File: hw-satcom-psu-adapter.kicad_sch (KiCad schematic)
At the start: 25 parts

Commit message: pmbus and normal
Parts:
- C1: value (none) -> 400uF/100V; footprint (none) -> Capacitor_THT:C_Disc_D5.0mm_W2.5mm_P5.00mm
- C2: value (none) -> 470uF/50V
- C3: value (none) -> 470uF/50V; footprint (none) -> Capacitor_THT:C_Disc_D5.0mm_W2.5mm_P5.00mm
- C4: value (none) -> 1uF/50V; footprint (none) -> Capacitor_SMD:C_0805_2012Metric
- D1: value (none) -> Yellow; footprint (none) -> LED_SMD:LED_0603_1608Metric
- D2, D3: footprint (none) -> LED_SMD:LED_0603_1608Metric
- F1: value (none) -> 10A; footprint (none) -> Fuse:Fuse_1206_3216Metric
- H1: value (none) -> MountingHole; footprint (none) -> MountingHole:MountingHole_2.5mm
- J1: value (none) -> Conn_01x04; footprint (none) -> Connector_PinSocket_2.54mm:PinSocket_1x04_P2.54mm_Vertical
- J2, J3: value (none) -> XT30; footprint (none) -> Connector_AMASS:AMASS_XT30PW-M_1x02_P2.50mm_Horizontal
- J4: value (none) -> Conn_01x06_MountingPin; footprint (none) -> Connector_Molex:Molex_CLIK-Mate_502382-0670_1x06-1MP_P1.25mm_Vertical
- J5: value (none) -> s; footprint (none) -> Connector_Molex:Molex_CLIK-Mate_502382-0370_1x03-1MP_P1.25mm_Vertical
- R1: value (none) -> 4.7k; footprint (none) -> Resistor_SMD:R_0603_1608Metric
- R10, R7, R8, R9: value (none) -> NC; footprint (none) -> Resistor_SMD:R_0603_1608Metric
- R2, R3: footprint (none) -> Resistor_SMD:R_0603_1608Metric
- R4: value (none) -> 3.9k; footprint (none) -> Resistor_SMD:R_0603_1608Metric
- R5: value (none) -> 100k; footprint (none) -> Resistor_SMD:R_0603_1608Metric
- R6: value (none) -> 47k; footprint (none) -> Resistor_SMD:R_0603_1608Metric
- U1: value (none) -> Brick-DCDC; footprint (none) -> alex's:Quarter-Brick-PMBus

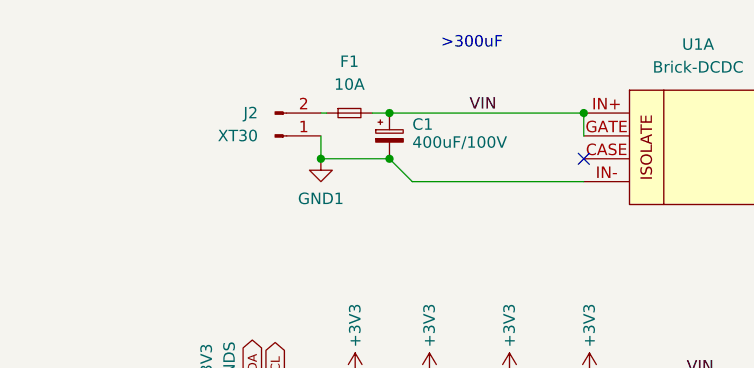
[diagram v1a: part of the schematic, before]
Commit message: change fuse footprint
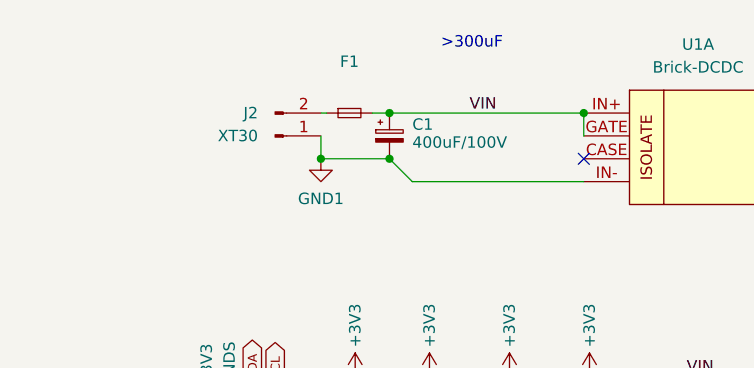
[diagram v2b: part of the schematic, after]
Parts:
- F1: value 10A -> (none); footprint Fuse:Fuse_1206_3216Metric -> (none)
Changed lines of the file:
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@@
     (in_bom yes) (on_board yes) (fields_autoplaced)
     (property "Reference" "F1" (id 0) (at 92.71 96.52 0))
-    (property "Value" "10A" (id 1) (at 92.71 99.06 0))
-    (property "Footprint" "Fuse:Fuse_1206_3216Metric" (id 2) (at 92.71 102.235 0)
+    (property "Value" "" (id 1) (at 92.71 99.06 0))
+    (property "Footprint" "" (id 2) (at 92.71 102.235 0)
       (effects (font (size 1.27 1.27)) hide)
     )
@@
     )
     (path "/3d21ad1e-adf2-4a6f-b9bb-fd727992bece"
-      (reference "F1") (unit 1) (value "10A") (footprint "Fuse:Fuse_1206_3216Metric")
+      (reference "F1") (unit 1) (value "10A") (footprint "Fuse:Fuse_2512_6332Metric")
     )
     (path "/d06f684c-b86b-49a5-ad3a-2b8c544739e6"

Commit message: Temp
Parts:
- removed D3: Yellow, LED_SMD:LED_0603_1608Metric, symbol Device:LED
- removed J2, J3: XT30, Connector_AMASS:AMASS_XT30PW-M_1x02_P2.50mm_Horizontal, symbol Connector:Conn_01x02_Male
- removed J4: Conn_01x06_MountingPin, Connector_Molex:Molex_CLIK-Mate_502382-0670_1x06-1MP_P1.25mm_Vertical, symbol Connector_Generic_MountingPin:Conn_01x06_MountingPin
- removed R5: 100k, Resistor_SMD:R_0603_1608Metric, symbol Device:R
- removed R6: 47k, Resistor_SMD:R_0603_1608Metric, symbol Device:R
- added C5: 47nF, lc:0402_C, symbol Device:C_Small
- added C6: 10nF, lc:0402_C, symbol Device:C_Small
- added D3: 1N4148WS, lc:SOD-323, symbol Diode:1N4148WS
- added D4, D5: Yellow, lc:0805_LED_S1_NUM, symbol Device:LED
- added D6, D7: 1N5819WS, lc:SOD-323, symbol Diode:1N4148WS
- added J2, J3, J4, J6, J8: Conn_01x04_Female, symbol Connector:Conn_01x04_Female
- added J7, J9: Conn_01x08_Female, symbol Connector:Conn_01x08_Female
- added Q1, Q2, Q3: NCE0140K2, Package_TO_SOT_SMD:TO-252-2, symbol Device:Q_NMOS_GDS
- added Q4, Q5: 2N7002, Package_TO_SOT_SMD:SOT-23, symbol Transistor_FET:2N7002
- added R11, R22: 8.2k, lc:0603_R, symbol Device:R_Small
- added R12, R17: 220k, lc:0603_R, symbol Device:R_Small
- added R13, R16, R18: 51k, lc:0603_R, symbol Device:R_Small
- added R14: 120k, lc:0603_R, symbol Device:R_Small
- added R15: 3m/1W, lc:2512_R, symbol Device:R_Small
- added R19, R23: 22k, lc:0603_R, symbol Device:R_Small
- added R20, R21: 5.1k, lc:0603_R, symbol Device:R_Small
- added R24: 10k, lc:0603_R, symbol Device:R_Small
- added R25: 390, lc:0603_R, symbol Device:R_Small
- added R26, R27: 100, lc:0603_R, symbol Device:R_Small
- added R5: 390k, lc:0603_R, symbol Device:R_Small
- added R6: 5.6k, lc:0603_R, symbol Device:R_Small
- added U10, U8, U9: ZXDN10, t123yh:ZXDN10, symbol t123yh:ZXDN10
- added U2: TPS2350, Package_SO:TSSOP-14_4.4x5mm_P0.65mm, symbol t123yh:TPS2350
- added U3, U4, U6: EL3H7(B)(TA)-G, Package_SO:SOP-4_4.4x2.6mm_P1.27mm, symbol Isolator:PC817
- added U5: AV10-48S05, t123yh:AV10-48Sxx, symbol t123yh:AV10-48S05
- added U7: TPS3510, Package_SO:SOIC-8_3.9x4.9mm_P1.27mm, symbol t123yh:TPS3510
- D2: value Yellow -> Red; footprint LED_SMD:LED_0603_1608Metric -> lc:0805_LED_S1_NUM
- F1: value (none) -> 10A; footprint (none) -> Fuse:Fuse_2512_6332Metric
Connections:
- net GND2: now also D5.1 (K), J8.1 (Pin_1), J8.2 (Pin_2), J8.3 (Pin_3), J8.4 (Pin_4), J9.1 (Pin_1), J9.2 (Pin_2), J9.3 (Pin_3), J9.4 (Pin_4), J9.5 (Pin_5), J9.6 (Pin_6), J9.7 (Pin_7), J9.8 (Pin_8), Q4.2 (S), Q5.2 (S), R19.2, R25.1, R26.1, R27.1, U10.3 (GND), U10.4 (GND), U4.2, U5.3 (-Vo), U7.2 (GND), U8.3 (GND), U8.4 (GND), U9.3 (GND), U9.4 (GND)
- net at J5.1 (Pin_1): no longer U1.6 (ISHARE)
- net at D2.1 (K): now also U2.2 (FLT)
- net GND1: no longer names the net of C1.2, U1.IN-
- net GND1: now also Q2.2 (D), R17.1, U5.1 (-Vin)
- removed net VIN: C1.1, D2.2 (A), F1.2, U1.GATE, U1.IN+
- net VOUT renamed +12V
- net +12V: now also D6.2 (A), J7.1 (Pin_1), J7.2 (Pin_2), J7.3 (Pin_3), J7.4 (Pin_4), J7.5 (Pin_5), J7.6 (Pin_6), J7.7 (Pin_7), J7.8 (Pin_8), R24.2, U10.2 (VIN), U8.2 (VIN), U9.2 (VIN)
- new net: D2.2 (A), R12.1
- new net: R18.1, U6.1
- new net: R27.2, U10.6 (ADJ)
- new net: Q5.3 (D), R24.1, U10.1 (EN), U8.1 (EN), U9.1 (EN)
- new net: R25.2, U8.6 (ADJ)
- new net: Q1.1 (G), U2.8 (GATEB)
- new net: C5.1, C6.1, D4.1 (K), Q1.2 (D), Q3.2 (D), R11.2, R15.2, U2.7 (SOURCE)
- new net: R11.1, R6.2, U2.4 (OV)
- new net: D3.1 (K), U2.1 (RTN)
- new net: R26.2, U9.6 (ADJ)
- new net: R17.2, U1.GATE, U3.3, U4.3
- new net: D6.1 (K), D7.1 (K), U7.7 (V_{DD})
- new net: D4.2 (A), R14.1
- new net: R16.2, U3.4, U4.4
- new net: Q2.3 (S), R15.1, U2.10 (SENSE)
- new net: D5.2 (A), R22.1
- new net: Q4.3 (D), R21.2, U7.1 (PGI)
- new net: Q2.1 (G), U2.11 (GAT)
- new net: R5.2, R6.1, U2.3 (UV)
- new net: C5.2, U2.5 (FLTTIM)
- new net: C6.2, U2.6 (RAMP)
- new net: Q3.1 (G), U2.9 (GATEA)
- new net: Q4.1 (G), R19.1, U6.3
- new net: R13.2, U3.1
- new net +3.3V: J6.1 (Pin_1), J6.2 (Pin_2), J6.3 (Pin_3), J6.4 (Pin_4), U7.5 (VS33), U8.5 (VOUT)
- new net +5VA: J3.1 (Pin_1), J3.2 (Pin_2), J3.3 (Pin_3), J3.4 (Pin_4), U7.6 (VS5), U9.5 (VOUT)
- new net +5VD: J4.1 (Pin_1), J4.2 (Pin_2), J4.3 (Pin_3), J4.4 (Pin_4), R23.1, U10.5 (VOUT)
- new net +5VSB: D7.2 (A), J2.1 (Pin_1), R20.1, R21.1, R22.2, U5.4 (+Vo), U6.4
- new net FPO: Q5.1 (G), R20.2, U4.1, U7.3 (~{FPO})
- new net NEGA: Q3.3 (S), U2.14 (-VINA)
- new net NEGB: Q1.3 (S), U2.13 (-VINB)
- new net PGOOD: J2.3 (Pin_3), R23.2, U7.8 (PGO)
- new net PG_HV: U2.12 (PG), U3.2, U6.2
- new net PSON: J2.2 (Pin_2), U7.4 (~{PSON})
- new net RET: C1.1, D3.2 (A), R12.2, R13.1, R14.2, R16.1, R18.2, R5.1, U1.IN+, U5.2 (+Vin)
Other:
- note added: "1W"
- note added: "Over voltage: 65V Under voltage: 41V"
- note added: "Pull up to always-on power"
- note added: "This octocoupler turns on when fault condition occurred downstream"
- note added: "This octocoupler turns on when power is not good"
- note added: "This octocoupler turns on when power is not good. When this happens, downstream PGOOD will be pulled low."
- note removed: ">1000uF"
- note removed: ">300uF"
- moved on the sheet: C1, C2, C3, C4, D1, H1, J1, J5, R1, R10, R2, R3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

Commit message: ATX
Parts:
- removed C2, C3: 470uF/50V, Capacitor_THT:C_Disc_D5.0mm_W2.5mm_P5.00mm, symbol Device:C_Polarized_Small
- removed C4: 1uF/50V, Capacitor_SMD:C_0805_2012Metric, symbol Device:C_Small
- removed F1: 10A, Fuse:Fuse_2512_6332Metric, symbol Device:Fuse_Small
- removed H1: MountingHole, MountingHole:MountingHole_2.5mm, symbol Mechanical:MountingHole
- removed J1: Conn_01x04, Connector_PinSocket_2.54mm:PinSocket_1x04_P2.54mm_Vertical, symbol Connector_Generic:Conn_01x04
- removed J2, J3, J4, J6, J8: Conn_01x04_Female, symbol Connector:Conn_01x04_Female
- removed J5: s, Connector_Molex:Molex_CLIK-Mate_502382-0370_1x03-1MP_P1.25mm_Vertical, symbol Connector_Generic_MountingPin:Conn_01x03_MountingPin
- removed J7, J9: Conn_01x08_Female, symbol Connector:Conn_01x08_Female
- removed R1, R2, R3: 4.7k, Resistor_SMD:R_0603_1608Metric, symbol Device:R
- removed R10, R9: NC, Resistor_SMD:R_0603_1608Metric, symbol Device:R_Small
- removed R4: 3.9k, Resistor_SMD:R_0603_1608Metric, symbol Device:R
- removed R7, R8: NC, Resistor_SMD:R_0603_1608Metric, symbol Device:R
- added C10, C12, C13, C15, C16, C17, C7, C8, C9: 470uF/25V, Capacitor_THT:CP_Radial_D6.3mm_P2.50mm, symbol Device:CP
- added C14: 100nF/100V, lc:0805_C, symbol Device:C_Small
- added D10, D8, D9: Green, lc:0805_LED_S1_NUM, symbol Device:LED
- added D11, D12: Blue, lc:0805_LED_S1_NUM, symbol Device:LED
- added FL1: ACM1513F-551T100, t123yh:ACM1513, symbol Device:Filter_EMI_LL_1423
- added H2, H3, H8, H9: SMTSO-M3, MountingHole:MountingHole_4.3mm_M4_Pad, symbol Mechanical:MountingHole
- added H4, H5, H6, H7: SMTSO-632, MountingHole:MountingHole_5.5mm_Pad, symbol Mechanical:MountingHole
- added J1, J5: Conn_01x02_Male, Connector_AMASS:AMASS_XT60-M_1x02_P7.20mm_Vertical, symbol Connector:Conn_01x02_Male
- added J2: ATX-24, t123yh:ATX-24P, symbol Connector:ATX-24
- added J3, J4: Conn_02x02_Top_Bottom, t123yh:ATX-4P, symbol Connector_Generic:Conn_02x02_Top_Bottom
- added J_CPU1, J_CPU2: Conn_02x04_Top_Bottom, t123yh:ATX-8P, symbol Connector_Generic:Conn_02x04_Top_Bottom
- added Q6: 2N7002, Package_TO_SOT_SMD:SOT-23, symbol Transistor_FET:2N7002
- added R1: 200k, lc:0402_R, symbol Device:R_Small
- added R2: 22k, lc:0402_R, symbol Device:R_Small
- added R3, R4: 56k, lc:0402_R, symbol Device:R_Small
- added R7, R8: 3.3k, lc:0402_R, symbol Device:R_Small
- D1: value Yellow -> Green; footprint LED_SMD:LED_0603_1608Metric -> lc:0805_LED_S1_NUM
- R11, R13, R19, R20, R21, R22, R23, R26, R27, R6: footprint lc:0603_R -> lc:0402_R
- R15: value 3m/1W -> 3m
- R16: value 51k -> 10k; footprint lc:0603_R -> lc:0402_R
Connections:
- net +12V: now also C10.1, C12.1, C13.1, C7.1, C8.1, J2.10 (+12V), J2.11 (+12V), J3.2 (Pin_2), J4.2 (Pin_2), J_CPU1.5 (Pin_5), J_CPU1.6 (Pin_6), J_CPU1.7 (Pin_7), J_CPU1.8 (Pin_8), J_CPU2.5 (Pin_5), J_CPU2.6 (Pin_6), J_CPU2.7 (Pin_7), J_CPU2.8 (Pin_8), R1.2
- net +3.3V: now also C15.1, J2.1 (+3.3V), J2.12 (+3.3V), J2.13 (+3.3V), J2.2 (+3.3V), R2.2
- net +5VA: now also R23.1, C16.1, J2.21 (+5V), J2.22 (+5V), J2.23 (+5V), J2.4 (+5V), J2.6 (+5V), R3.2, R7.2, R8.2
- net +5VD: now also C17.1, J3.3 (Pin_3), J4.3 (Pin_3), R4.2; no longer R23.1
- net +5VSB: now also C9.1, J2.9 (+5VSB)
- net GND2: now also D1.1 (K), C10.2, C12.2, C13.2, C15.2, C16.2, C17.2, C7.2, C8.2, C9.2, D10.1 (K), D8.1 (K), D9.1 (K), J2.15 (GND), J2.17 (GND), J2.18 (GND), J2.19 (GND), J2.24 (GND), J2.3 (GND), J2.5 (GND), J2.7 (GND), J3.1 (Pin_1), J3.4 (Pin_4), J4.1 (Pin_1), J4.4 (Pin_4), J_CPU1.1 (Pin_1), J_CPU1.2 (Pin_2), J_CPU1.3 (Pin_3), J_CPU1.4 (Pin_4), J_CPU2.1 (Pin_1), J_CPU2.2 (Pin_2), J_CPU2.3 (Pin_3), J_CPU2.4 (Pin_4), Q6.2 (S)
- net NEGA: now also J1.1 (Pin_1)
- net NEGB: now also J5.1 (Pin_1)
- net PGOOD: now also J2.8 (PWR_OK), Q6.1 (G)
- net PSON: now also D12.1 (K), J2.16 (PS_ON#)
- net NEG_FIL: now reaches C1.2, R17.1, U1.IN-, U5.1 (-Vin)
- net NEG_FIL: now also FL1.4; no longer Q2.2 (D)
- net DCDC_EN: now reaches Q5.3 (D), R24.1, U10.1 (EN), U8.1 (EN), U9.1 (EN)
- net NEG: now reaches C5.1, C6.1, D4.1 (K), Q1.2 (D), Q3.2 (D), R11.2, R15.2, U2.7 (SOURCE)
- net +3V3: no longer names the net of D1.2 (A)
- net +3V3: now also R1.1
- net RET renamed RTN
- net RTN: now also C14.1, FL1.2, J1.2 (Pin_2), J5.2 (Pin_2); no longer C1.1, R18.2, U1.IN+, U5.2 (+Vin)
- new net: D12.2 (A), R8.1
- new net: D8.2 (A), R2.1
- new net: D11.1 (K), Q6.3 (D)
- new net: D11.2 (A), R7.1
- new net: D10.2 (A), R4.1
- new net: D9.2 (A), R3.1
- new net NEG_SS: C14.2, FL1.1, Q2.2 (D)
- new net RTN_FIL: C1.1, FL1.3, R18.2, U1.IN+, U5.2 (+Vin)
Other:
- note added: "(back)"
- note added: "Lenovo HDD Cable"
- note removed: "1W"
- moved on the sheet: C5, C6, D2, D3, D4, Q1, Q2, Q3, R11, R12, R13, R14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

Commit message: TPS2350
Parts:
- added D13, D14: SMCJ60A, Diode_SMD:D_SMC, symbol Diode:SMF5V0A
- added R9: 56k, lc:0603_R, symbol Device:R_Small
- R14: value 120k -> 56k
- R7, R8: value 3.3k -> 4.7k
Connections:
- net NEG: now also Q1.3 (S), Q3.3 (S); no longer D4.1 (K), Q1.2 (D), Q3.2 (D)
- net NEGA: now also Q3.2 (D), D13.2 (A2); no longer Q3.3 (S)
- net NEGB: now also Q1.2 (D), D14.2 (A2); no longer Q1.3 (S)
- net RTN: now also D13.1 (A1), D14.1 (A1)
- net at Q2.3 (S), R15.1, U2.10 (SENSE): now also R9.1
- new net: D4.1 (K), R9.2
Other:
- moved on the sheet: J1, J5

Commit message: LM5067
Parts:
- removed C5: 47nF, lc:0402_C, symbol Device:C_Small
- removed C6: 10nF, lc:0402_C, symbol Device:C_Small
- removed D14: SMCJ60A, Diode_SMD:D_SMC, symbol Diode:SMF5V0A
- removed D2: Red, lc:0805_LED_S1_NUM, symbol Device:LED
- removed D3: 1N4148WS, lc:SOD-323, symbol Diode:1N4148WS
- removed J5: Conn_01x02_Male, Connector_AMASS:AMASS_XT60-M_1x02_P7.20mm_Vertical, symbol Connector:Conn_01x02_Male
- removed Q1, Q3: NCE0140K2, Package_TO_SOT_SMD:TO-252-2, symbol Device:Q_NMOS_GDS
- removed U2: TPS2350, Package_SO:TSSOP-14_4.4x5mm_P0.65mm, symbol t123yh:TPS2350
- added C2: 470nF, lc:0402_C, symbol Device:C_Small
- added C3: 100nF, lc:0805_C, symbol Device:C_Small
- added R10: 56k, lc:0402_R, symbol Device:R_Small
- added U2: LM5067, Package_SO:MSOP-10_3x3mm_P0.5mm, symbol t123yh:LM5067
- D13: value SMCJ60A -> SMCJ70A
- J1: value Conn_01x02_Male -> XT60
- Q2: value NCE0140K2 -> KIA3510AD
- R11: value 8.2k -> 4.7k
- R12: value 220k -> 10k; footprint lc:0603_R -> lc:1206_R
- R13, R16: footprint lc:0402_R -> lc:0603_R
- R15: value 3m -> 4m
- R5: value 390k -> 130k
- R6: value 5.6k -> 4.7k
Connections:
- net NEGA is gone; now on net VEE: D13.2 (A2), J1.1 (Pin_1)
- net NEG_SS: now also R9.1, U2.9 (OUT)
- net PG_HV: now also U2.10 (~{PGD})
- net RTN: now also R12.1, R13.2, R18.1; no longer R12.2, R13.1
- net RTN_FIL: no longer R18.2
- net at U6.1: now also R18.2; no longer R18.1
- net at R11.1, R6.2: now also U2.3 (OVP)
- net at Q2.3 (S), R15.1: now also U2.7 (SENSE); no longer R9.1
- net at Q2.1 (G): now also U2.8 (GATE)
- net at R5.2, R6.1: now also U2.2 (UVLO)
- net at U3.1: now also R13.1; no longer R13.2
- net NEG renamed VEE
- net VEE: now also C2.2, C3.1, R10.1, U2.5 (VEE)
- new net: C3.2, R12.2, U2.1 (VCC)
- new net: C2.1, U2.6 (TIMER)
- new net: R10.2, U2.4 (PWR)
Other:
- note added: "Over voltage: 71-74V Under voltage: 37-39V"
- note removed: "Over voltage: 65V Under voltage: 41V"
- moved on the sheet: D13, J1, Q2, R11, R13, R15, R18, R5, R6

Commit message: Layout improvements
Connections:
- net +12V: now also J_CPU1.1 (Pin_1), J_CPU1.2 (Pin_2), J_CPU1.3 (Pin_3), J_CPU1.4 (Pin_4), J_CPU2.1 (Pin_1), J_CPU2.2 (Pin_2), J_CPU2.3 (Pin_3), J_CPU2.4 (Pin_4); no longer J_CPU1.5 (Pin_5), J_CPU1.6 (Pin_6), J_CPU1.7 (Pin_7), J_CPU1.8 (Pin_8), J_CPU2.5 (Pin_5), J_CPU2.6 (Pin_6), J_CPU2.7 (Pin_7), J_CPU2.8 (Pin_8)
- net GND2: now also J_CPU1.5 (Pin_5), J_CPU1.6 (Pin_6), J_CPU1.7 (Pin_7), J_CPU1.8 (Pin_8), J_CPU2.5 (Pin_5), J_CPU2.6 (Pin_6), J_CPU2.7 (Pin_7), J_CPU2.8 (Pin_8); no longer J_CPU1.1 (Pin_1), J_CPU1.2 (Pin_2), J_CPU1.3 (Pin_3), J_CPU1.4 (Pin_4), J_CPU2.1 (Pin_1), J_CPU2.2 (Pin_2), J_CPU2.3 (Pin_3), J_CPU2.4 (Pin_4)
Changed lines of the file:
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@@
     (pin "1")
   )
-  (symbol (lib_id "Connector_Generic:Conn_02x04_Top_Bottom") (at 306.07 176.53 0) (unit 1)
+  (symbol (lib_id "Connector_Generic:Conn_02x04_Top_Bottom") (at 308.61 176.53 0) (mirror y) (unit 1)
     (in_bom yes) (on_board yes) (fields_autoplaced)
     (property "Reference" "J_CPU1" (id 0) (at 307.34 167.64 0))
     (property "Value" "Conn_02x04_Top_Bottom" (id 1) (at 307.34 170.18 0))
-    (property "Footprint" "t123yh:ATX-8P" (id 2) (at 306.07 176.53 0)
-      (effects (font (size 1.27 1.27)) hide)
-    )
-    (property "Datasheet" "~" (id 3) (at 306.07 176.53 0)
+    (property "Footprint" "t123yh:ATX-8P" (id 2) (at 308.61 176.53 0)
+      (effects (font (size 1.27 1.27)) hide)
+    )
+    (property "Datasheet" "~" (id 3) (at 308.61 176.53 0)
       (effects (font (size 1.27 1.27)) hide)
     )
@@
     )
   )
-  (symbol (lib_id "Connector_Generic:Conn_02x04_Top_Bottom") (at 306.07 199.39 0) (unit 1)
+  (symbol (lib_id "Connector_Generic:Conn_02x04_Top_Bottom") (at 308.61 199.39 0) (mirror y) (unit 1)
     (in_bom yes) (on_board yes) (fields_autoplaced)
     (property "Reference" "J_CPU2" (id 0) (at 307.34 190.5 0))
     (property "Value" "Conn_02x04_Top_Bottom" (id 1) (at 307.34 193.04 0))
-    (property "Footprint" "t123yh:ATX-8P" (id 2) (at 306.07 199.39 0)
-      (effects (font (size 1.27 1.27)) hide)
-    )
-    (property "Datasheet" "~" (id 3) (at 306.07 199.39 0)
-      (effects (font (size 1.27 1.27)) hide)
-    )
+    (property "Footprint" "t123yh:ATX-8P" (id 2) (at 308.61 199.39 0)
+      (effects (font (size 1.27 1.27)) hide)
+    )
+    (property "Datasheet" "~" (id 3) (at 308.61 199.39 0)
+      (effects (font (size 1.27 1.27)) hide)
+    )

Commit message: Fix
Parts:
- removed Q4: 2N7002, Package_TO_SOT_SMD:SOT-23, symbol Transistor_FET:2N7002
- added C11, C4, C5, C6: 100nF/100V, lc:0805_C, symbol Device:C_Small
- added R28: 100k, lc:0402_R, symbol Device:R_Small
- D1: renamed from D8; footprint lc:0805_LED_S1_NUM -> lc:0603_LED_S1_NUM
- D10, D11, D12, D4, D5, D9: footprint lc:0805_LED_S1_NUM -> lc:0603_LED_S1_NUM
- D8: renamed from D1; footprint lc:0805_LED_S1_NUM -> lc:0603_LED_S1_NUM
- H2, H3, H8, H9: footprint MountingHole:MountingHole_4.3mm_M4_Pad -> t123yh:MountingHole_SMTSO-M3
- H4, H5, H6, H7: footprint MountingHole:MountingHole_5.5mm_Pad -> t123yh:MountingHole_SMTSO-632
- J_CPU1, J_CPU2: footprint t123yh:ATX-8P -> t123yh:ATX-8P-Square
- R13: value 51k -> 27k; footprint lc:0603_R -> lc:0805_R
- R16: value 10k -> 1k
- R17: value 220k -> 1k
- R18: value 51k -> 5.1k; footprint lc:0603_R -> lc:0402_R
- R20: value 5.1k -> 3.3k
- R21: value 5.1k -> 10k
- R7, R8: value 4.7k -> 5.1k
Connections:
- net +5VSB: now also R18.1; no longer U6.4
- net FPO: now also R18.2, U4.2, R28.2; no longer Q5.1 (G), R20.2, U4.1
- net GND2: now also C6.2; no longer U4.2
- net NEG_FIL: now also C4.2, C5.2; no longer R17.1
- net PG_HV: now also R13.1, R16.2, R17.2; no longer U3.2, U6.2
- net RTN: now also C11.1; no longer R16.1, R18.1
- net RTN_FIL: now also C5.1
- net VEE: now also U3.2, U6.2, C11.2
- net at U6.1: now also R17.1; no longer R18.2
- net at D6.1 (K), D7.1 (K), U7.7 (V_{DD}): now also C6.1
- net at R21.2: now also U6.4; no longer U7.1 (PGI)
- net at R19.1, U6.3: now also U7.1 (PGI)
- net at U3.1: now also R16.1; no longer R13.1
- net NEG_SS renamed GND1
- net GND1: now also U4.3
- new net: R20.2, U4.1
- new net: Q5.1 (G), R28.1
- new net: U3.3, U4.4
- new net GATE: C4.1, U1.GATE, U3.4
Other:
- note added: "LM5067 PGD High: Good Low: Starting / Not Good"
- note added: "This octocoupler turns off when power is not good. In this case, downstream PG will be pulled low."
- note added: "This octocoupler turns on when downstream is enabled"
- note added: "This octocoupler turns on when power is good"
- note removed: "Pull up to always-on power"
- note removed: "This octocoupler turns on when fault condition occurred downstream"
- note removed: "This octocoupler turns on when power is not good"
- note removed: "This octocoupler turns on when power is not good. When this happens, downstream PGOOD will be pulled low."
- moved on the sheet: C1, C10, C12, C13, C14, C15, C16, C17, C2, C3, C7, C8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
